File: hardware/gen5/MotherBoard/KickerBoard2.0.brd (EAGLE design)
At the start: 143.9 x 141.8 mm, 155 parts, among them Q2 IXFH6N90, Q3 IXFH6N90

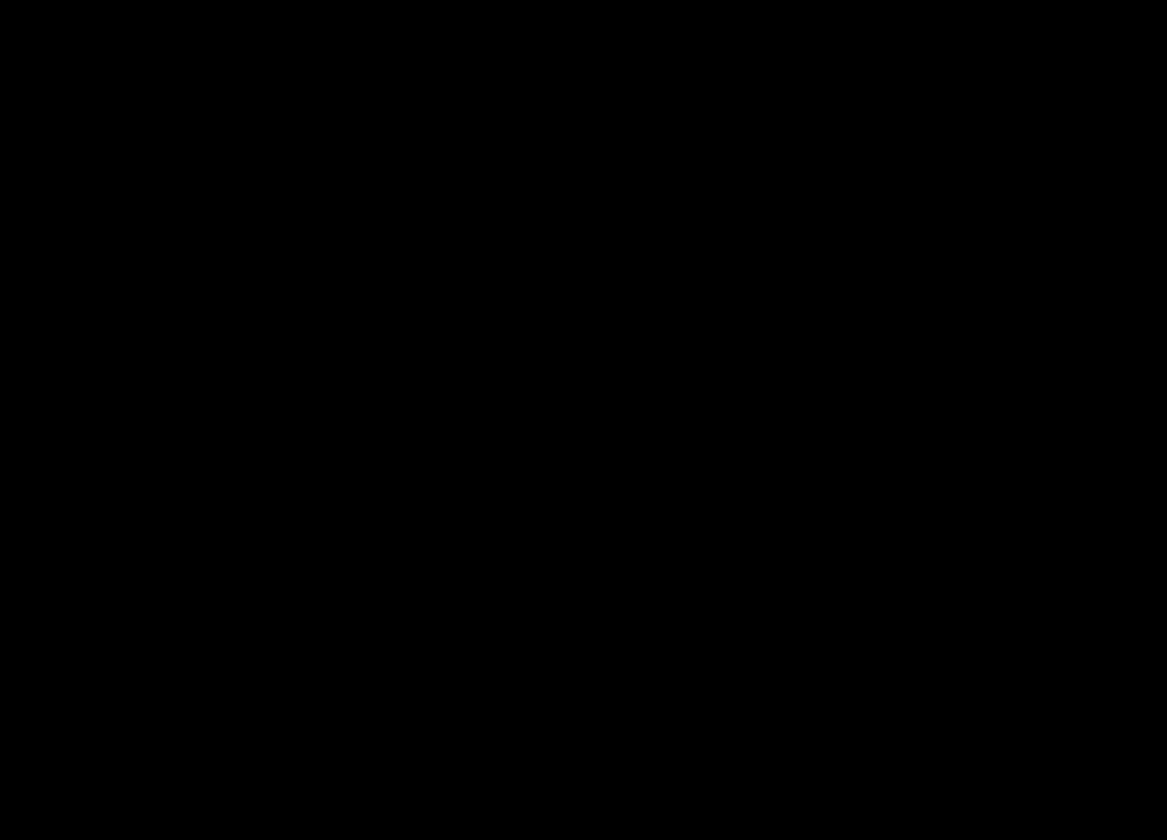
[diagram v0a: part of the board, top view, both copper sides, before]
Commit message: new motor controller
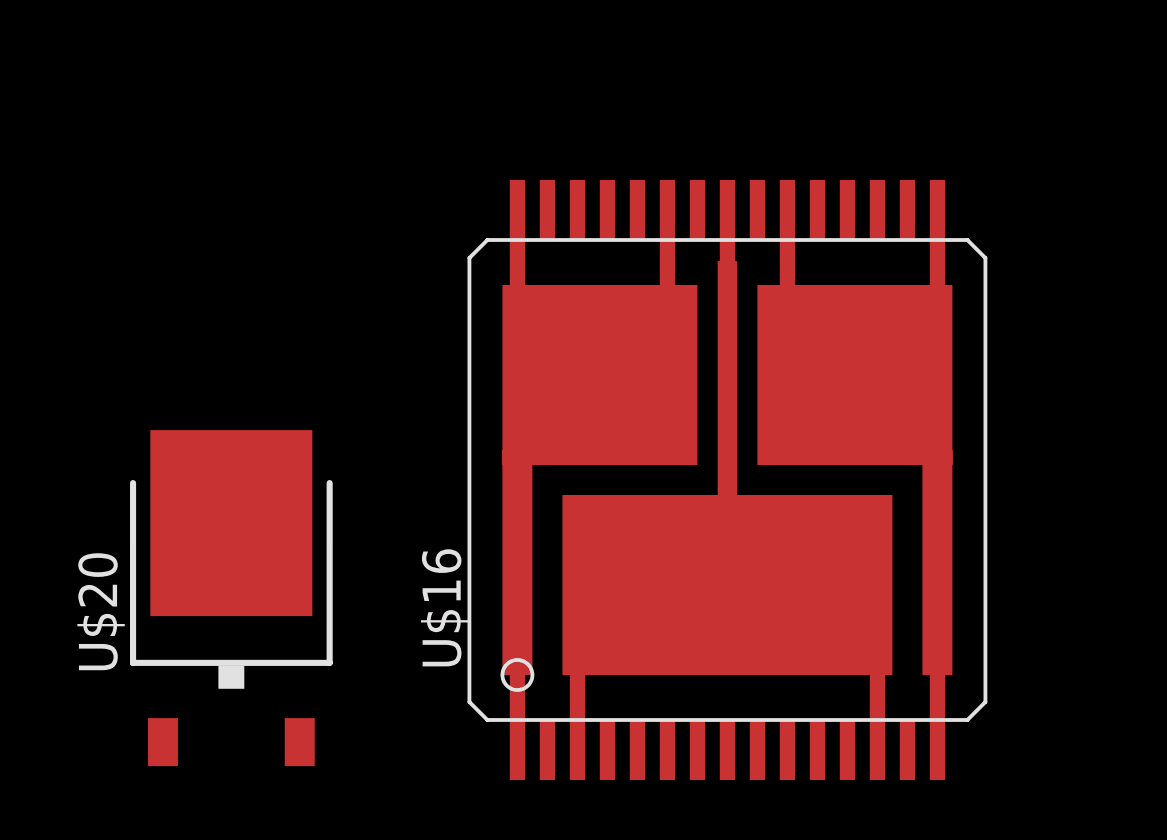
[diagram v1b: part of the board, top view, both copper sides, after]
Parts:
- added U$16: VNH5019, IAD-Library:MULTIPOWERSO-30
- added U$20: MOSFET-NCH, IAD-Library:TO252-3
